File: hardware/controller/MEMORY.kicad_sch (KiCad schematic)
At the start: 0 parts

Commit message: added memory and fixed gpio pins
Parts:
- added IC3: W25Q256JVEIQ, SON127P800X600X80-9N-D, symbol SamacSys_Parts:W25Q256JVEIQ
- added J5: 4677, SOIC127P600X175-8N, symbol SamacSys_Parts:4677
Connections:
- new net +3V3: IC3.8 (VCC), J5.8 (VCC)
- new net GND: IC3.4 (GND), IC3.9 (EP), J5.4 (VSS)
- new net MEM.SIO0: IC3.5 (DI_(IO0)), J5.5 (SI/SIO[0])
- new net MEM.SIO1: IC3.2 (DO_(IO1)_1), J5.2 (SO/SIO[1])
- new net MEM.SIO2: IC3.3 (DO_(IO1)_2), J5.3 (SIO[2])
- new net MEM.SIO3: IC3.7 (IO3), J5.7 (SIO[3])
- new net MEM.SPICLK: IC3.6 (CLK), J5.6 (SCLK)
- new net MEM.~{CE}: J5.1 (CE#)
- new net MEM.~{CS}: IC3.1 (/CS)
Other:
- note added: "PSRAM and Flash"

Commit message: modified power circuitry
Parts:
- IC3: footprint SON127P800X600X80-9N-D -> SamacSys_Parts:SON127P800X600X80-9N-D
- IC7: renamed from J5; footprint SOIC127P600X175-8N -> SamacSys_Parts:SOIC127P600X175-8N
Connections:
- net MEM.SPICLK renamed MEM.SCK
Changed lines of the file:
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@@
 	)
 	(bus_entry
-		(at 38.1 48.26)
+		(at 66.04 72.39)
 		(size 2.54 2.54)
 		(stroke
@@
 	)
 	(bus_entry
-		(at 38.1 33.02)
+		(at 66.04 57.15)
 		(size 2.54 2.54)
 		(stroke
@@
 	)
 	(bus_entry
-		(at 38.1 40.64)
+		(at 66.04 64.77)
 		(size 2.54 2.54)
 		(stroke
@@
 	)
 	(bus_entry
-		(at 38.1 35.56)
+		(at 66.04 59.69)
 		(size 2.54 2.54)
 		(stroke
@@
 	)
 	(bus_entry
-		(at 38.1 43.18)
+		(at 66.04 67.31)
 		(size 2.54 2.54)
 		(stroke
@@
 	)
 	(bus_entry
-		(at 38.1 45.72)
+		(at 66.04 69.85)
 		(size 2.54 2.54)
 		(stroke
@@
 	)
 	(bus_entry
-		(at 38.1 35.56)
+		(at 66.04 59.69)
 		(size 2.54 2.54)
 		(stroke
@@
 	)
 	(bus_entry
-		(at 38.1 38.1)
+		(at 66.04 62.23)
 		(size 2.54 2.54)
 		(stroke
@@
 	(wire
 		(pts
-			(xy 40.64 35.56) (xy 46.99 35.56)
+			(xy 68.58 59.69) (xy 74.93 59.69)
 		)
 		(stroke
@@
 	(bus
 		(pts
-			(xy 38.1 33.02) (xy 38.1 35.56)
+			(xy 66.04 57.15) (xy 66.04 59.69)
 		)
 		(stroke
@@
 	(wire
 		(pts
-			(xy 40.64 40.64) (xy 46.99 40.64)
+			(xy 68.58 64.77) (xy 74.93 64.77)
 		)
 		(stroke
@@
 	(wire
 		(pts
-			(xy 40.64 38.1) (xy 46.99 38.1)
+			(xy 68.58 62.23) (xy 74.93 62.23)
 		)
 		(stroke
@@
 	(bus
 		(pts
-			(xy 38.1 35.56) (xy 38.1 38.1)
+			(xy 66.04 59.69) (xy 66.04 62.23)
 		)
 		(stroke
@@
 	(wire
 		(pts
-			(xy 40.64 43.18) (xy 46.99 43.18)
+			(xy 68.58 67.31) (xy 74.93 67.31)
 		)
 		(stroke
@@
 	(bus
 		(pts
-			(xy 38.1 45.72) (xy 38.1 48.26)
+			(xy 66.04 69.85) (xy 66.04 72.39)
 		)
 		(stroke
@@
 	(wire
 		(pts
-			(xy 40.64 48.26) (xy 46.99 48.26)
+			(xy 68.58 72.39) (xy 74.93 72.39)
 		)
 		(stroke
@@
 	(bus
 		(pts
-			(xy 38.1 43.18) (xy 38.1 45.72)
+			(xy 66.04 67.31) (xy 66.04 69.85)
 		)
 		(stroke
@@
 	(wire
 		(pts
-			(xy 40.64 50.8) (xy 46.99 50.8)
+			(xy 68.58 74.93) (xy 74.93 74.93)
 		)
 		(stroke
@@
 	(wire
 		(pts
-			(xy 40.64 45.72) (xy 46.99 45.72)
+			(xy 68.58 69.85) (xy 74.93 69.85)
 		)
 		(stroke
@@
 	(bus
 		(pts
-			(xy 38.1 40.64) (xy 38.1 43.18)
+			(xy 66.04 64.77) (xy 66.04 67.31)
 		)
 		(stroke
@@
 	(bus
 		(pts
-			(xy 38.1 38.1) (xy 38.1 40.64)
+			(xy 66.04 62.23) (xy 66.04 64.77)
 		)
 		(stroke
@@
 	)
 	(label "MEM.SIO3"
-		(at 46.99 35.56 0)
+		(at 74.93 59.69 0)
 		(effects
 			(font
@@
 	)
 	(label "MEM.SIO0"
-		(at 46.99 43.18 0)
+		(at 74.93 67.31 0)
 		(effects
 			(font
@@
 		)
 	)
-	(label "MEM.MEMSPICLK"
-		(at 46.99 50.8 0)
+	(label "MEM.SCK"
+		(at 74.93 74.93 0)
 		(effects
 			(font
@@
 	)
 	(label "MEM.~{CS}"
-		(at 46.99 48.26 0)
+		(at 74.93 72.39 0)
 		(effects
 			(font
@@
 	)
 	(label "MEM.SIO1"
-		(at 46.99 40.64 0)
+		(at 74.93 64.77 0)
 		(effects
 			(font
@@
 		)
 	)
-	(label "MEM.SPICLK"
+	(label "MEM.SCK"
 		(at 160.02 73.66 0)
 		(effects
@@
 	)
 	(label "MEM.~{CE}"
-		(at 46.99 45.72 0)
+		(at 74.93 69.85 0)
 		(effects
 			(font
@@
 		)
 	)
-	(label "MEM.SPICLK"
+	(label "MEM.SCK"
 		(at 160.02 95.25 0)
 		(effects
@@
 	)
 	(label "MEM.SIO2"
-		(at 46.99 38.1 0)
+		(at 74.93 62.23 0)
 		(effects
 			(font
@@
 	(hierarchical_label "MEM{MEMORY}"
 		(shape bidirectional)
-		(at 38.1 33.02 180)
+		(at 66.04 57.15 180)
 		(effects
 			(font
@@
 			)
 		)
-		(property "Footprint" "SON127P800X600X80-9N-D"
+		(property "Footprint" "SamacSys_Parts:SON127P800X600X80-9N-D"
 			(at 156.21 185.09 0)
 			(effects
@@
 		(dnp no)
 		(fields_autoplaced yes)
-		(property "Reference" "J5"
+		(property "Reference" "IC7"
 			(at 139.7 60.96 0)
 			(effects
@@
 			)
 		)
-		(property "Footprint" "SOIC127P600X175-8N"
+		(property "Footprint" "SamacSys_Parts:SOIC127P600X175-8N"
 			(at 156.21 163.5 0)
 			(effects
@@
 			(project "controller"
 				(path "/869bea87-c885-4ead-826b-3f34ceacafad/0e7b3f4d-646f-4949-ba8d-4e4489aa7d1d"
-					(reference "J5")
+					(reference "IC7")
 					(unit 1)
 				)

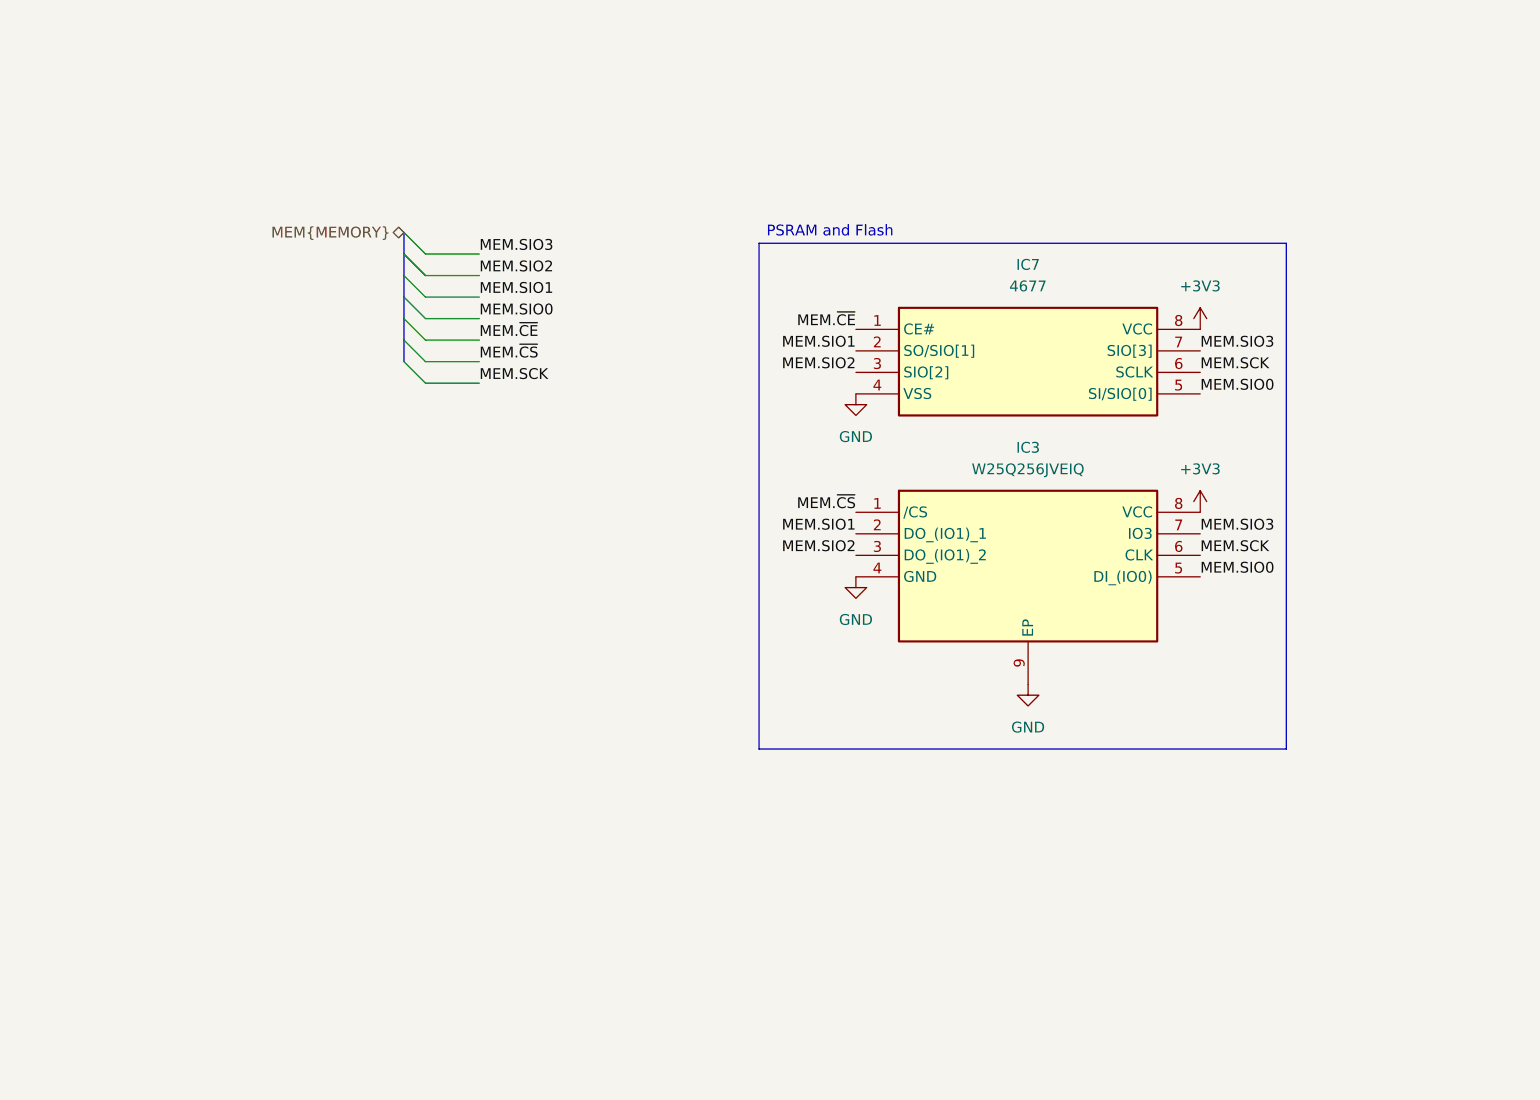
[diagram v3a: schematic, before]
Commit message: finished first rev of controller schematic minus actually finding passive components. moved some features to rev2 todo
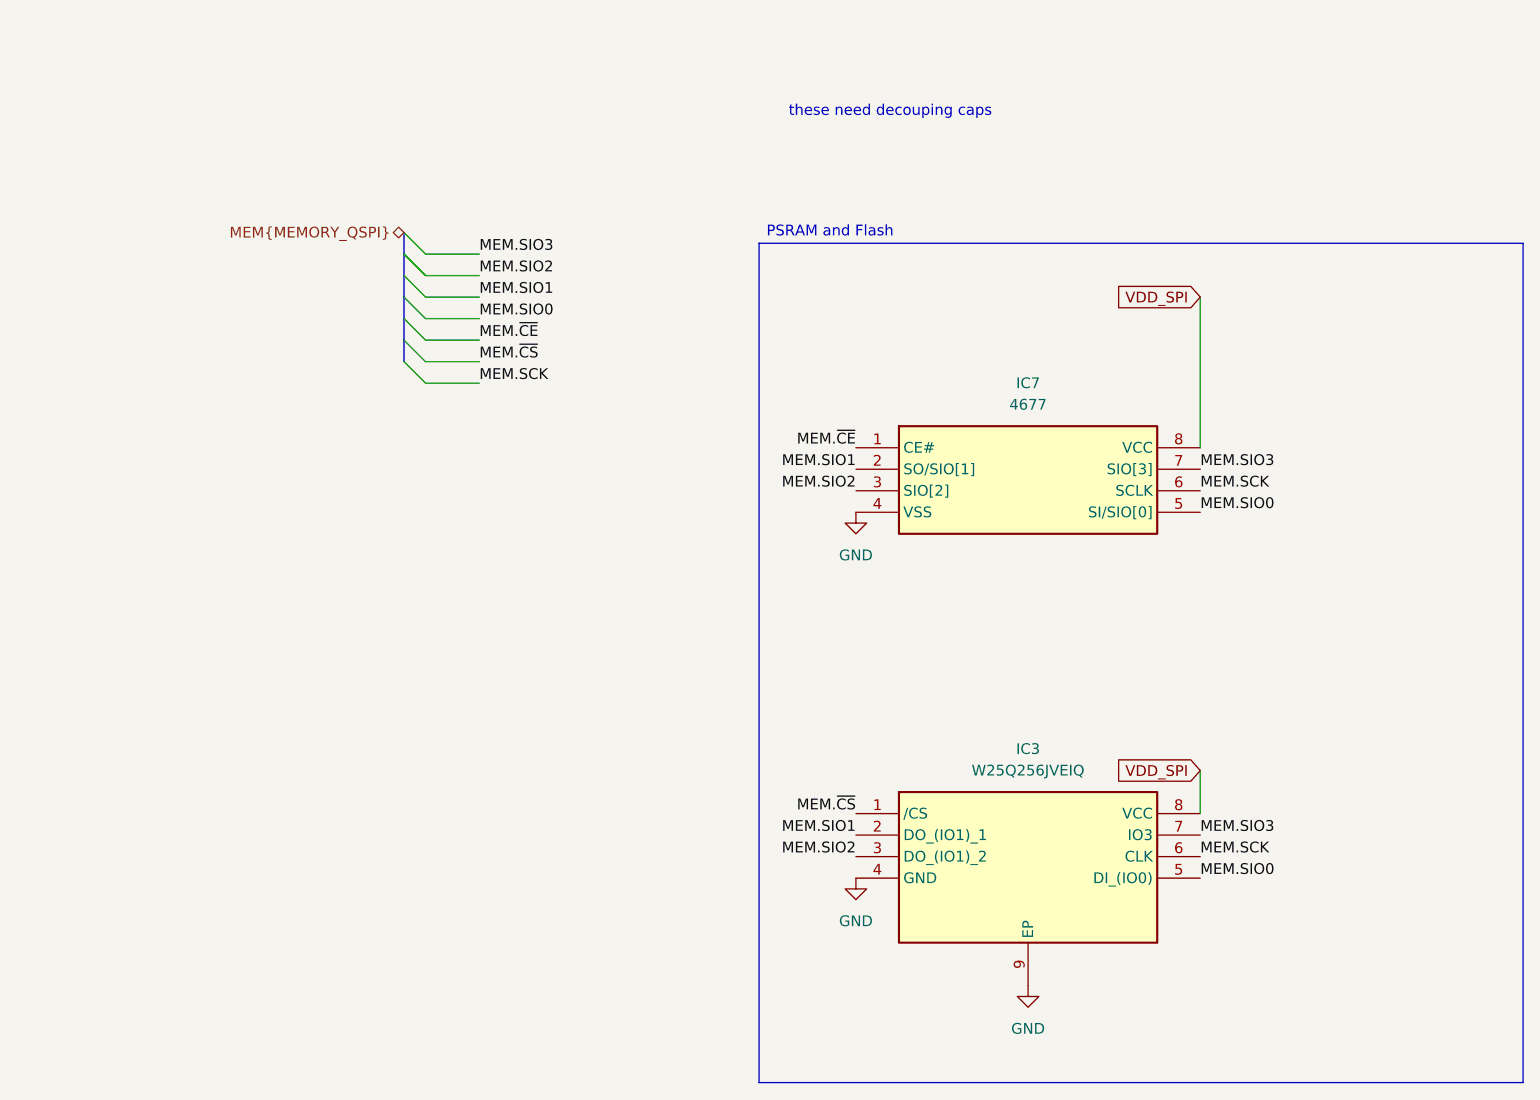
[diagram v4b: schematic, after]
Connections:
- net +3V3 renamed VDD_SPI
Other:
- note added: "these need decouping caps"
- moved on the sheet: IC3, IC7

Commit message: Moved LEDs around. Replaced some discrete resistors with resistor arrays. Added mounting holes. Added. Added a lot of actual components for passive elements
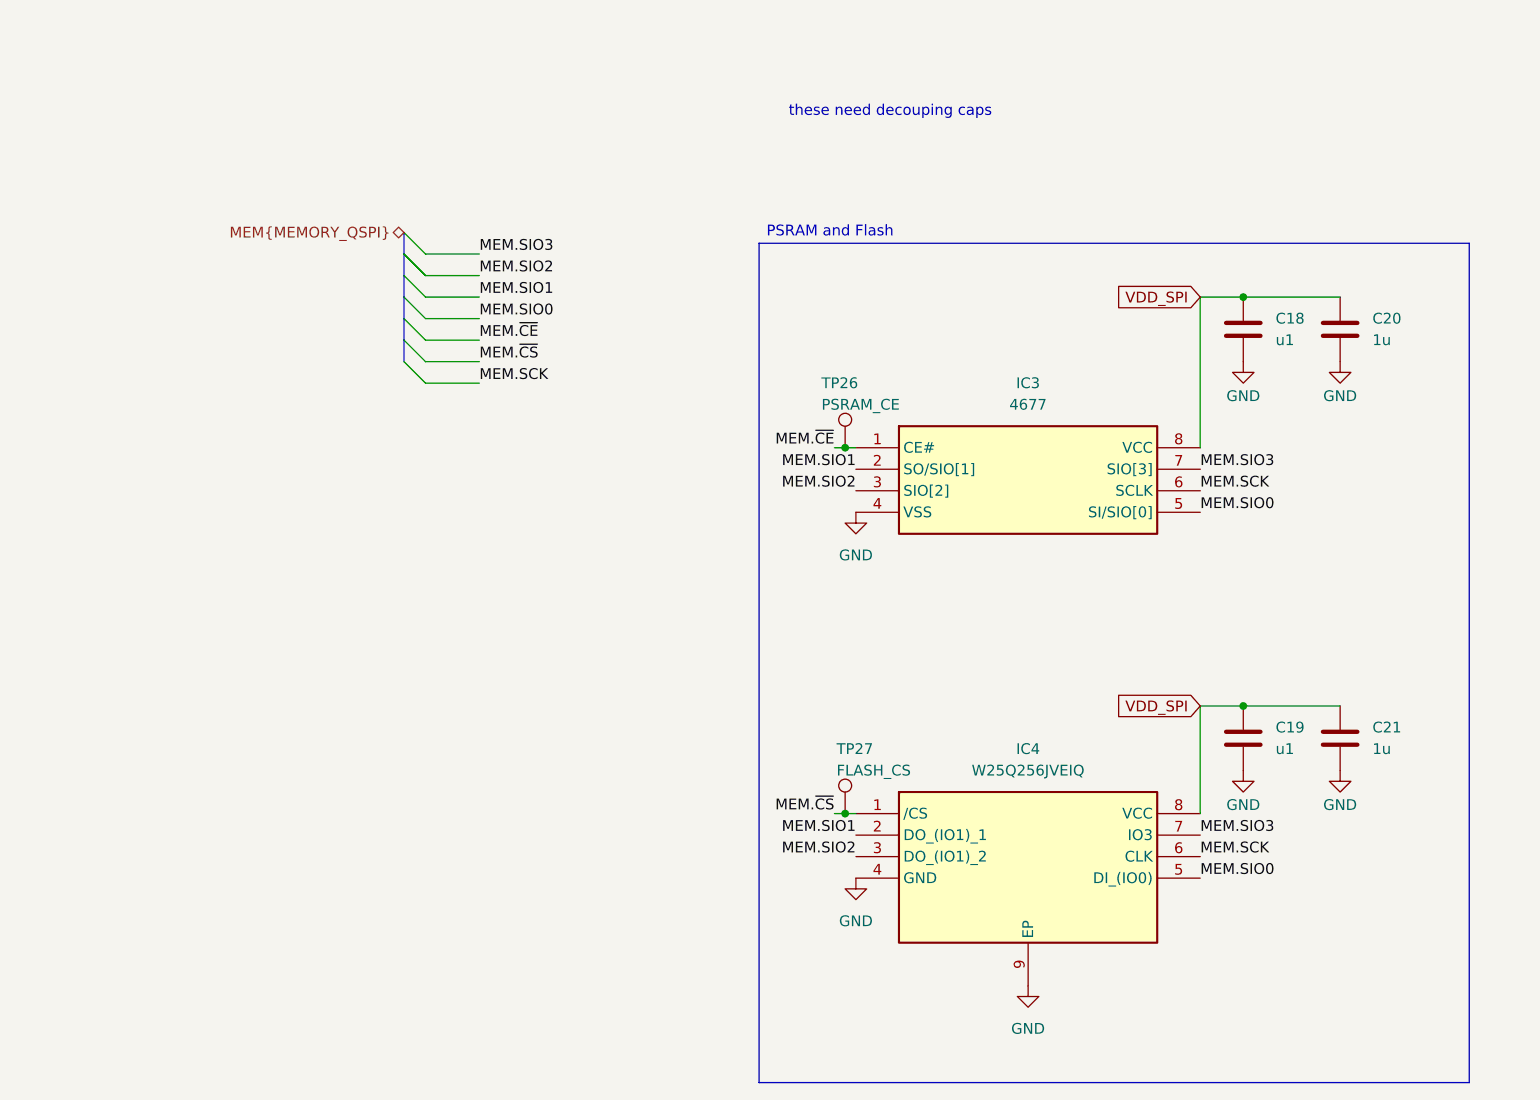
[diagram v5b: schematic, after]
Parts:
- added C18, C19: u1, MAJx16, symbol Device:C
- added C20, C21: 1u, CAPC2012X135N, symbol Device:C
- added TP26: PSRAM_CE, TestPoint:TestPoint_Pad_1.0x1.0mm, symbol Connector:TestPoint
- added TP27: FLASH_CS, TestPoint:TestPoint_Pad_1.0x1.0mm, symbol Connector:TestPoint
- IC3: renamed from IC7; footprint SamacSys_Parts:SOIC127P600X175-8N -> SOIC127P600X175-8N
- IC4: renamed from IC3; footprint SamacSys_Parts:SON127P800X600X80-9N-D -> SON127P800X600X80-9N-D
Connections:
- net GND: now also C18.2, C19.2, C20.2, C21.2
- net MEM.~{CE}: now also TP26.1
- net MEM.~{CS}: now also TP27.1
- net VDD_SPI: now also C18.1, C19.1, C20.1, C21.1
